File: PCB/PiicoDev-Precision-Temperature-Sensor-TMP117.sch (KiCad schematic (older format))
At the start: 23 parts, among them J1 , J2 , J3 , U1 TMP117

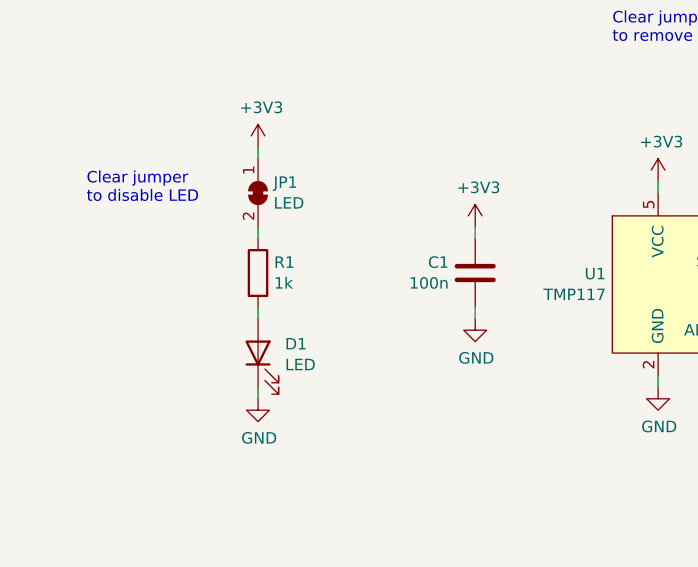
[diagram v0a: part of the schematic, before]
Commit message: Update R1 to 4k7
New LED is more efficient, use larger resistor. Optimise 1k out of the BOM
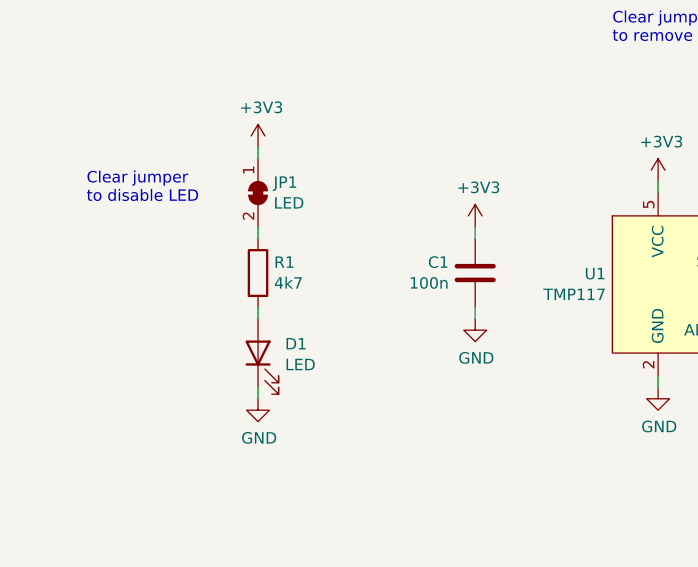
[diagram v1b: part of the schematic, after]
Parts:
- R1: value 1k -> 4k7
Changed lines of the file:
@@
 P 2900 3750
 F 0 "R1" H 2970 3796 50  0000 L CNN
-F 1 "1k" H 2970 3705 50  0000 L CNN
+F 1 "4k7" H 2970 3705 50  0000 L CNN
 F 2 "Resistor_SMD:R_0402_1005Metric" V 2830 3750 50  0001 C CNN
 F 3 "~" H 2900 3750 50  0001 C CNN

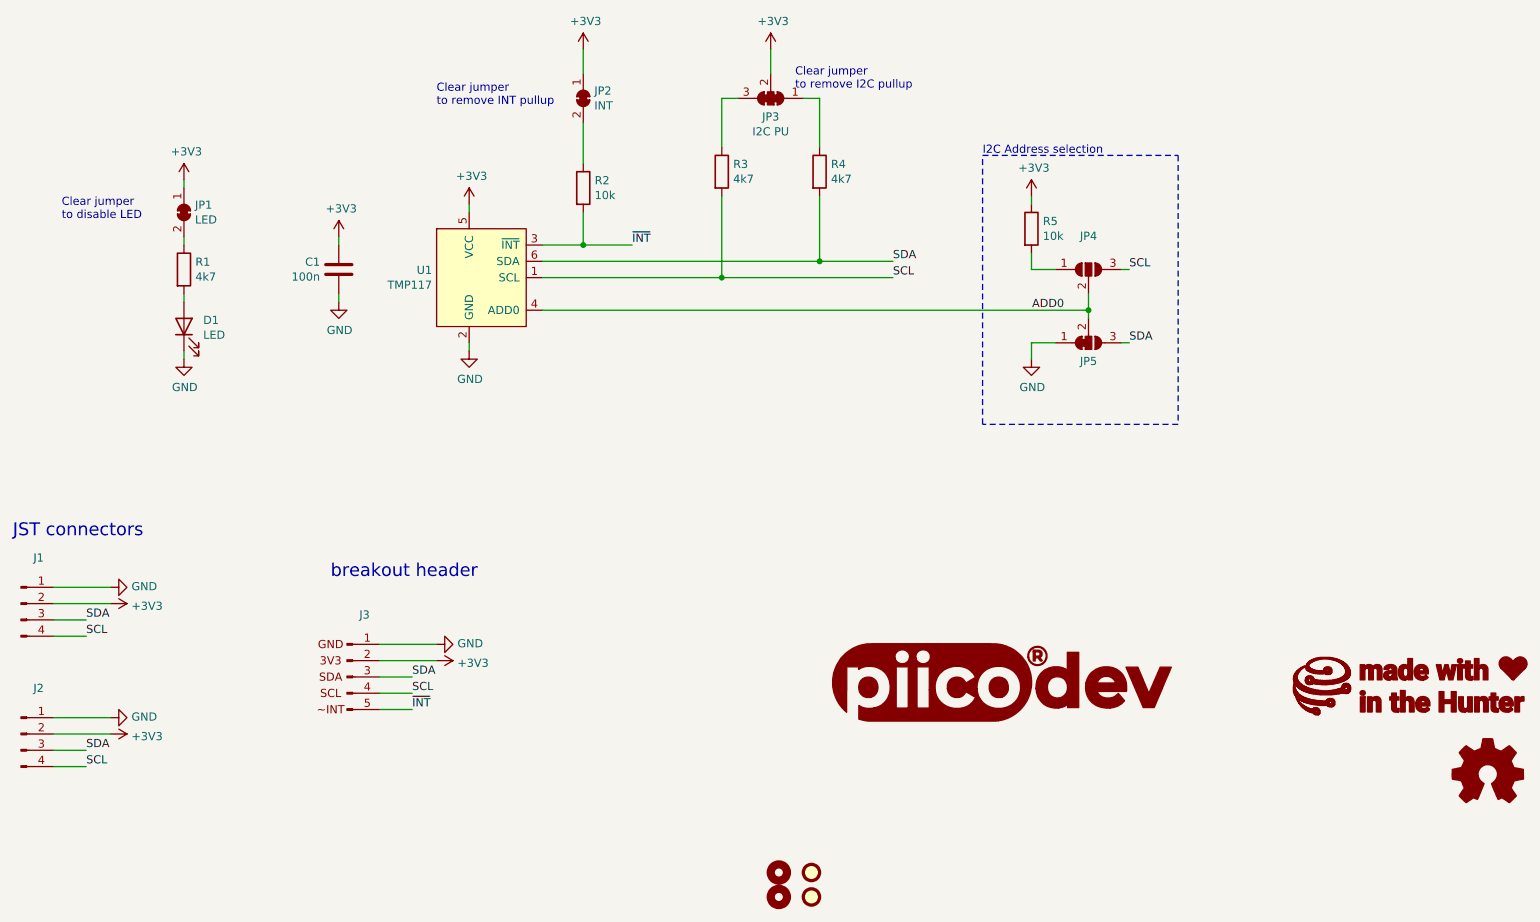
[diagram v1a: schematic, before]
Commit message: v11 Update
Change resistor values
Add DIP switch and remove ADR jumper
Update graphic labels
Remove solder mask between jumper pads
Update text formatting
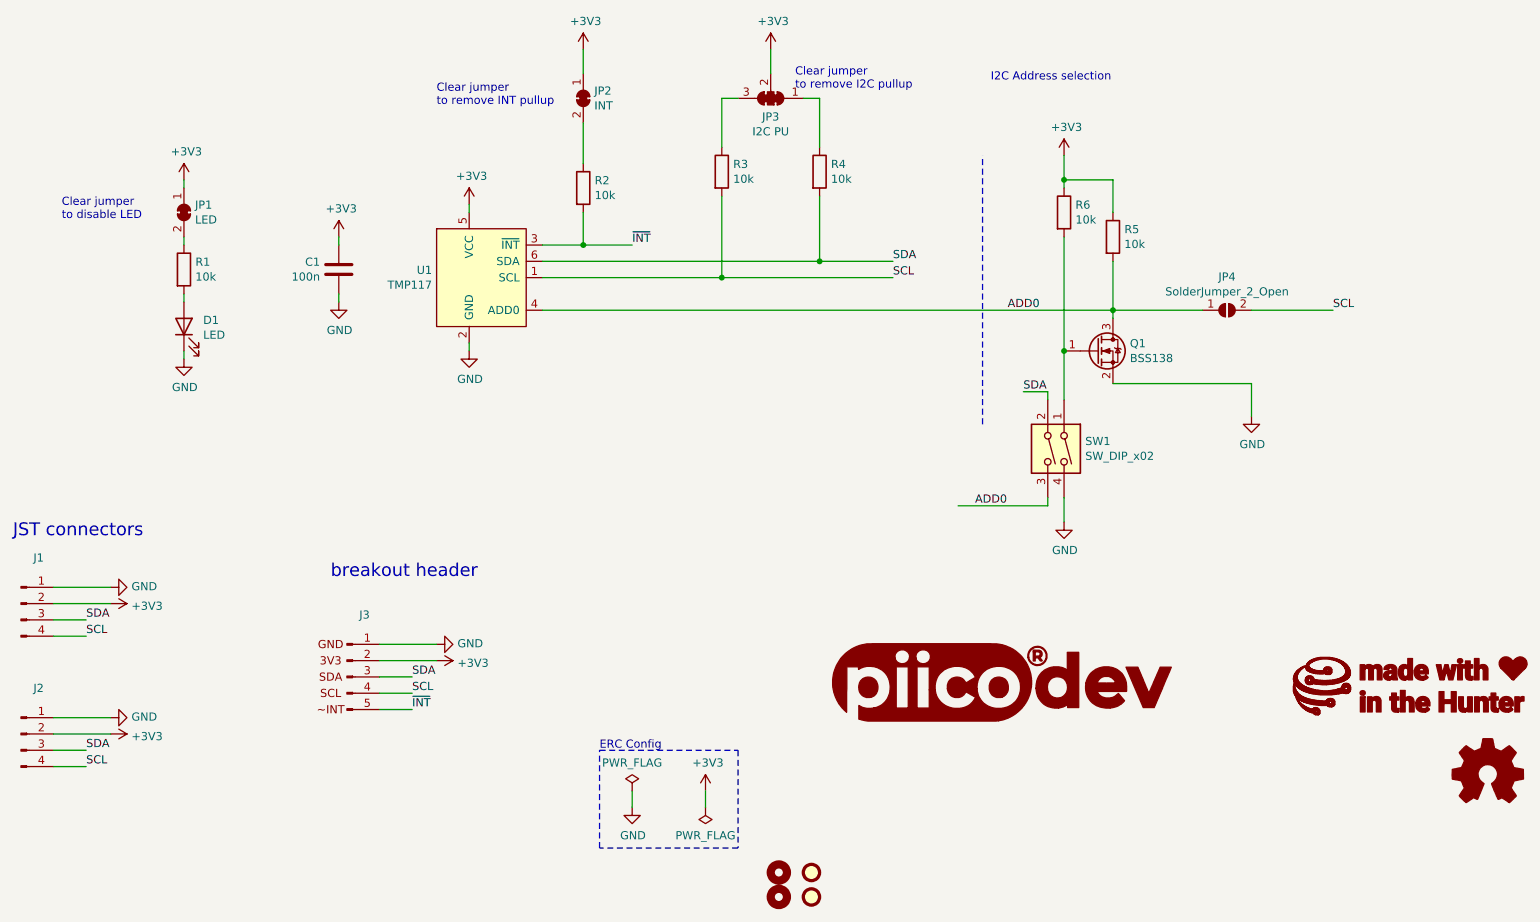
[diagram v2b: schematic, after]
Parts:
- removed G1: LOGO_CoreElectronics_made-with-love, PiicoDev_Artwork:piicodev_logo_14.2x3.4mm, symbol CoreElectronics_Artwork:LOGO_CoreElectronics_made-with-love
- removed JP4: (no value), Jumper:SolderJumper-3_P1.3mm_Open_RoundedPad1.0x1.5mm, symbol Jumper:SolderJumper_3_Open
- removed JP5: (no value), Jumper:SolderJumper-3_P1.3mm_Bridged12_RoundedPad1.0x1.5mm, symbol Jumper:SolderJumper_3_Bridged12
- added G1: LOGO_CoreElectronics_no-text, CoreElectronics_Artwork:CoreElectronics_logo_5mm, symbol CoreElectronics_Artwork:LOGO_CoreElectronics_no-text
- added G3: LOGO_made-with-love, CoreElectronics_Artwork:piicodev_logo_14.2x3.4mm, symbol CoreElectronics_Artwork:LOGO_made-with-love
- added JP4: SolderJumper_2_Open, CoreElectronics_Components:SolderJumper-2_P1.3mm_Open_RoundedPad1.0x1.5mm, symbol Jumper:SolderJumper_2_Open
- added Q1: BSS138, Package_TO_SOT_SMD:SOT-23, symbol Transistor_FET:BSS138
- added R6: 10k, Resistor_SMD:R_0402_1005Metric, symbol Device:R
- added SW1: SW_DIP_x02, CoreElectronics_Components:SW_DIP_x02_Slide_CHS-02A1, symbol Switch:SW_DIP_x02
- G2: footprint Piico_Artwork:piicodev_logo_14.2x3.4mm -> CoreElectronics_Artwork:piicodev_logo_14.2x3.4mm
- JP1, JP2: footprint Jumper:SolderJumper-2_P1.3mm_Bridged_RoundedPad1.0x1.5mm -> CoreElectronics_Components:SolderJumper-2_P1.3mm_Bridged_RoundedPad1.0x1.5mm
- R1, R3, R4: value 4k7 -> 10k
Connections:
- net +3V3: now also R6.1
- net ADD0: now also R5.2, JP4.1 (A), Q1.3 (D), SW1.3
- net GND: now also Q1.2 (S), SW1.4
- net SCL: now also JP4.2 (B)
- net SDA: now also SW1.2
- new net: Q1.1 (G), R6.2, SW1.1
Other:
- note added: "ERC Config"
- moved on the sheet: R5

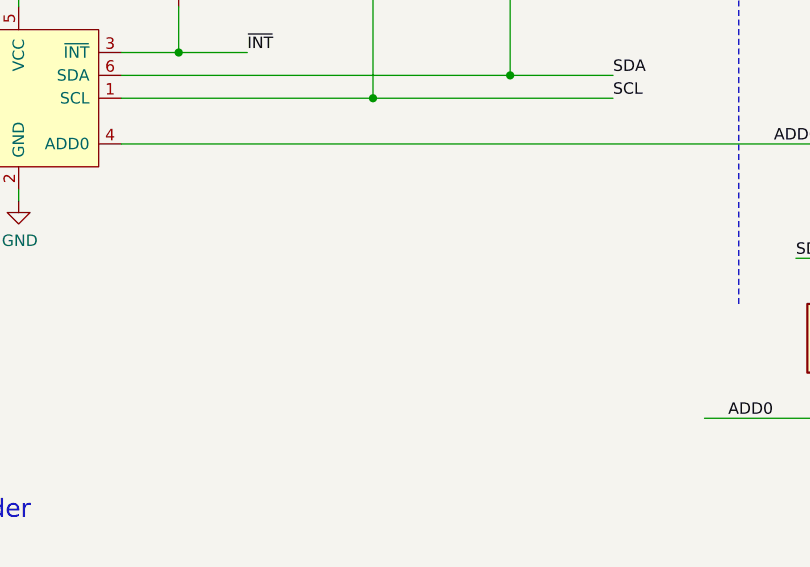
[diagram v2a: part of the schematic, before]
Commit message: v12 Update
Migrate to KiCad 6.0
Add 120R resistor
Add 4-bit DIP SW
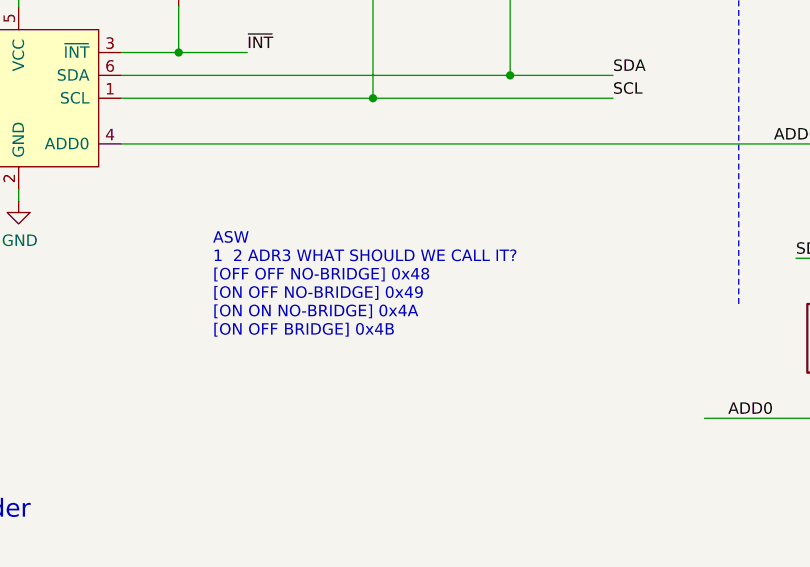
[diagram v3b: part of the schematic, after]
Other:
- note added: "ASW\n1 2 ADR3 WHAT SHOULD WE CALL IT?\n[OFF OFF NO-BRIDGE] 0x48\n[ON OFF NO-BRIDGE] 0x49\n[ON ON NO-BRIDGE] 0x4A\n[ON OFF BRIDGE] 0x4B"
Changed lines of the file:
@@
 	1    0    0    -1
 $EndComp
+Text Notes 5500 4850 0    50   ~ 0
+ASW\n1  2 ADR3 WHAT SHOULD WE CALL IT?\n[OFF OFF NO-BRIDGE] 0x48\n[ON OFF NO-BRIDGE] 0x49\n[ON ON NO-BRIDGE] 0x4A\n[ON OFF BRIDGE] 0x4B
 $EndSCHEMATC
